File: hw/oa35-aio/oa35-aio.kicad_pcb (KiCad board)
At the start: 6 copper layers, 36 x 36 mm, 283 parts, among them J1 TYPE-C-31-M-12, J10 M1A, J11 M1B, J12 M1C, J13 M2A, J14 M2B, J15 M2C, J16 M3A, J17 M3B, J18 M3C, J19 M4A, J2 SM06B-SRSS-TB, J20 M4B, J21 M4C, J3 BAT+, J4 BAT-, P1 +5V, P10 TX6, P11 RX1, P12 TX1, P13 LED, P14 BZ-, P15 BZ+, P16 RSSI, P17 SCL, P18 SDA, P19 +3V3, P2 GND, P20 GND, P21 VBAT, P22 GND, P3 RX2, P4 TX2, P5 +5V, P6 GND, P7 RX4, P8 TX4, P9 RX6, Q1 2N7002, U1 INA186A3IDCKR, U10 USBLC6-2SC6, U2 LMR51430YFDDCR, U20 AT32F421G8U7, U21 NSG2065Q, U3 LMR51430YFDDCR, U30 AT32F421G8U7, U31 NSG2065Q, U4 LP5912-3.3DRVR, U40 AT32F421G8U7, U41 NSG2065Q, U5 TLV76733DRVR, U50 AT32F421G8U7, U51 NSG2065Q, U6 STM32F722RET6, U7 ICM-42688-P, U8 BMP280, U9 W25Q128JVSIQ, Y1 8MHz

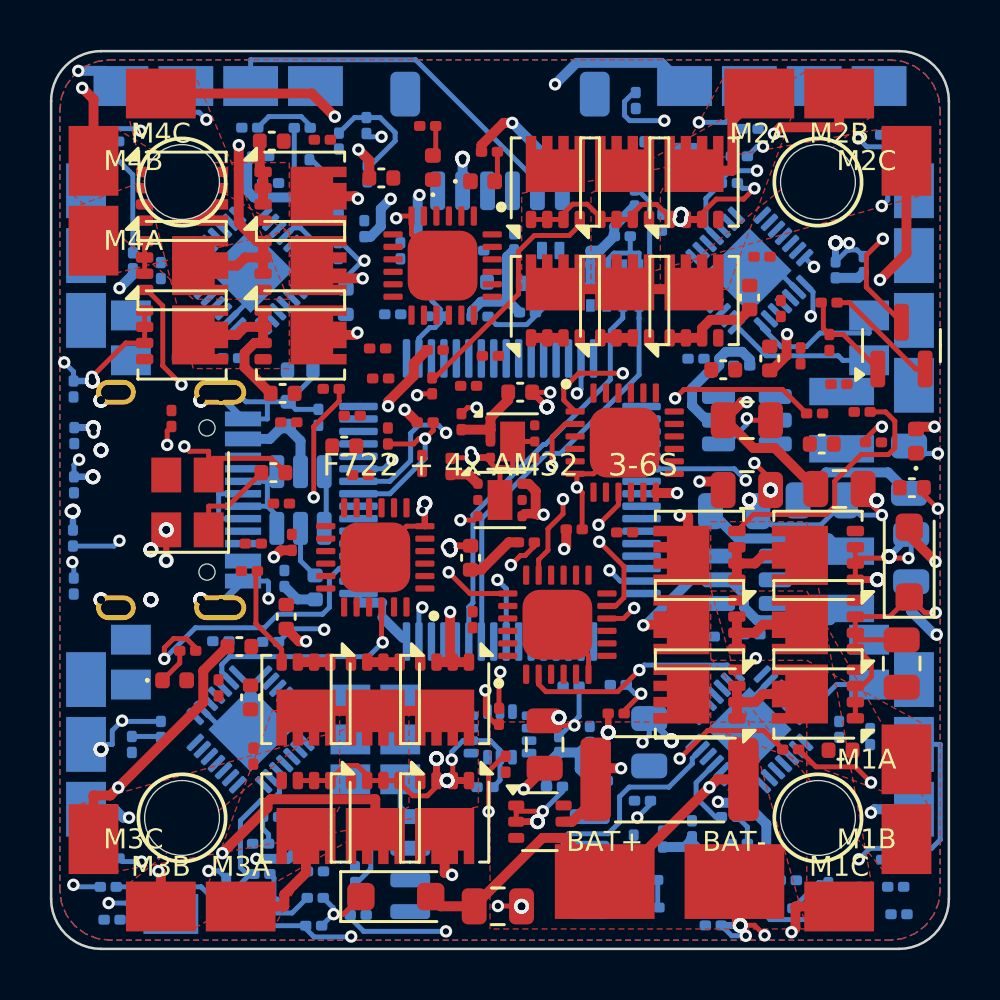
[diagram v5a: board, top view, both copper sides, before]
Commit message: OA35-AIO: leave the router's net classes alone, widen the power nets after
Rewriting the DSN class block to ask for wider phase and supply traces was
what made freerouting give up: with the rewritten block it routed 85 nets out
of 279, with KiCad's own block it routes them all. The high-current nets get
their copper back afterwards instead -- stitch.widen() fattens each segment
to as much as 0.8 mm wherever the surrounding geometry allows, testing the
widened shape against every other net before committing.

Co-Authored-By: Claude Opus 5 <noreply@anthropic.com>
Claude-Session: https://claude.ai/code/session_013J1rgXZWykCJN7jVVS67P2
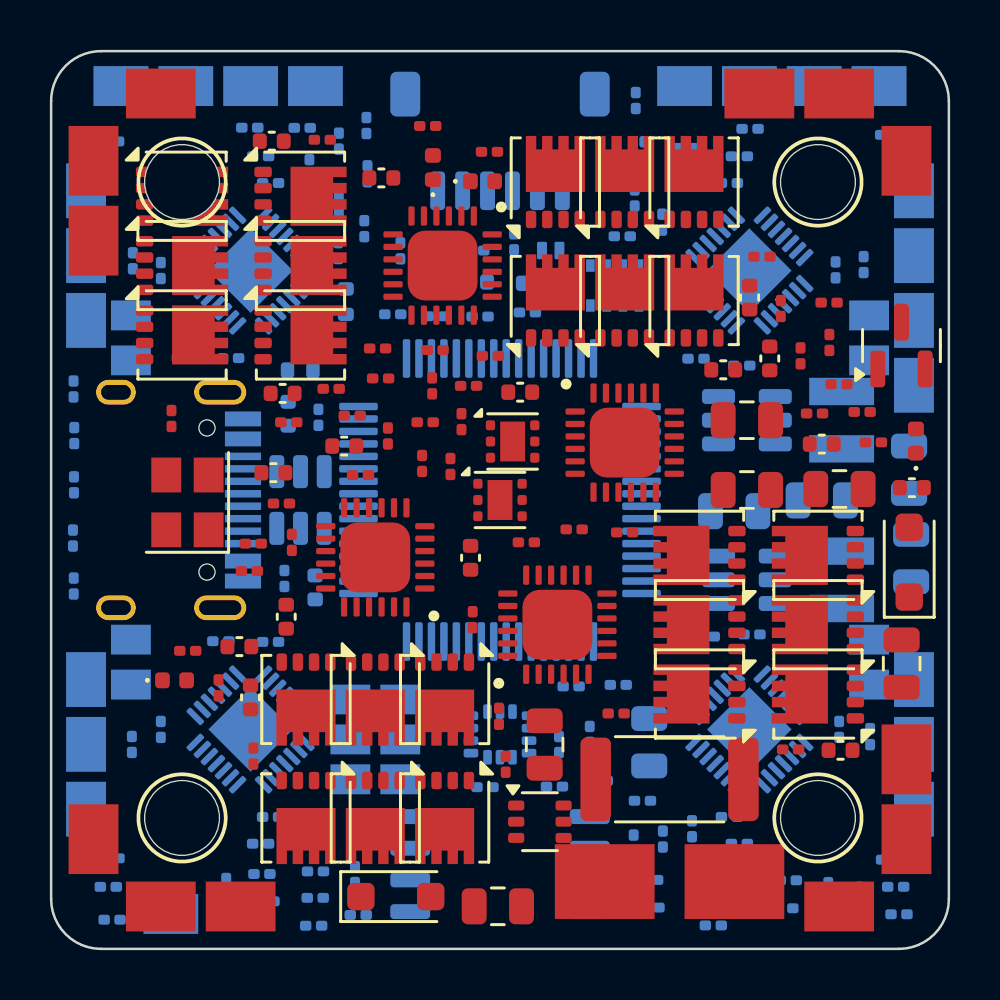
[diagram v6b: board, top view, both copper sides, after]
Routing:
- net GND: track 231.8 -> 0.00 mm, vias 129 -> 0
- net +5V: track 84.6 -> 0.00 mm, vias 6 -> 0
- net +3V3: track 46.5 -> 0.00 mm, vias 2 -> 0
- net PH_C_3: track 45.4 -> 0.00 mm, vias 4 -> 0
- net VBAT: track 45.0 -> 0.00 mm, vias 16 -> 0
- net PAD_BZ-: track 42.9 -> 0.00 mm, vias 2 -> 0
- net CURR: track 37.7 -> 0.00 mm, vias 3 -> 0
- net PAD_RSSI: track 37.3 -> 0.00 mm, vias 2 -> 0
- net ADC_RSSI: track 31.8 -> 0.00 mm, vias 2 -> 0
- net VBAT_IN: track 30.9 -> 0.00 mm, vias 2 -> 0
- net PH_B_4: track 30.1 -> 0.00 mm, vias 4 -> 0
- net PH_C_4: track 27.0 -> 0.00 mm, vias 2 -> 0
- net PH_B_3: track 26.1 -> 0.00 mm, vias 3 -> 0
- net PH_B_2: track 23.7 -> 0.00 mm, vias 2 -> 0
- net FBB_2: track 23.2 -> 0.00 mm, vias 2 -> 0
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- removed copper zone on B.Cu, net GND
- removed copper zone on F.Cu, net GND
- removed copper zone on In1.Cu, net GND
- removed copper zone on In3.Cu, net GND
- removed copper zone on In4.Cu, net GND
- removed copper zone on F.Cu, net PH_A_1
- removed copper zone on F.Cu, net PH_A_2
- removed copper zone on F.Cu, net PH_A_3
- removed copper zone on F.Cu, net PH_A_4
- removed copper zone on F.Cu, net PH_B_1
- removed copper zone on F.Cu, net PH_B_2
- removed copper zone on F.Cu, net PH_B_3
- removed copper zone on F.Cu, net PH_B_4
- removed copper zone on F.Cu, net PH_C_1
- removed copper zone on F.Cu, net PH_C_2
- removed copper zone on F.Cu, net PH_C_3
- removed copper zone on F.Cu, net PH_C_4
- removed copper zone on In2.Cu, net VBAT
- removed copper zone on F.Cu, net VBAT_IN
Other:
- board text removed: "+3V3"
- board text removed: "+5V"
- board text removed: "BAT+"
- board text removed: "BAT-"
- board text removed: "BOOT0"
- board text removed: "BZ+"
- board text removed: "BZ-"
- board text removed: "F722 + 4x AM32 3-6S"
- board text removed: "GND"
- board text removed: "LED"
- board text removed: "M1A"
- board text removed: "M1B"
- board text removed: "M1C"
- board text removed: "M2A"
- board text removed: "M2B"
- board text removed: "M2C"
- board text removed: "M3A"
- board text removed: "M3B"
- board text removed: "M3C"
- board text removed: "M4A"
- board text removed: "M4B"
- board text removed: "M4C"
- board text removed: "NRST"
- board text removed: "OA35-AIO rev A"
- board text removed: "RSSI"
- board text removed: "RX1"
- board text removed: "RX2"
- board text removed: "RX4"
- board text removed: "RX6"
- board text removed: "SCL"
- board text removed: "SDA"
- board text removed: "SWCLK"
- board text removed: "SWCLK1"
- board text removed: "SWCLK2"
- board text removed: "SWCLK3"
- board text removed: "SWCLK4"
- board text removed: "SWDIO"
- board text removed: "SWDIO1"
- board text removed: "SWDIO2"
- board text removed: "SWDIO3"
- board text removed: "SWDIO4"
- board text removed: "TX1"
- board text removed: "TX2"
- board text removed: "TX4"
- board text removed: "TX6"
- board text removed: "VBAT"

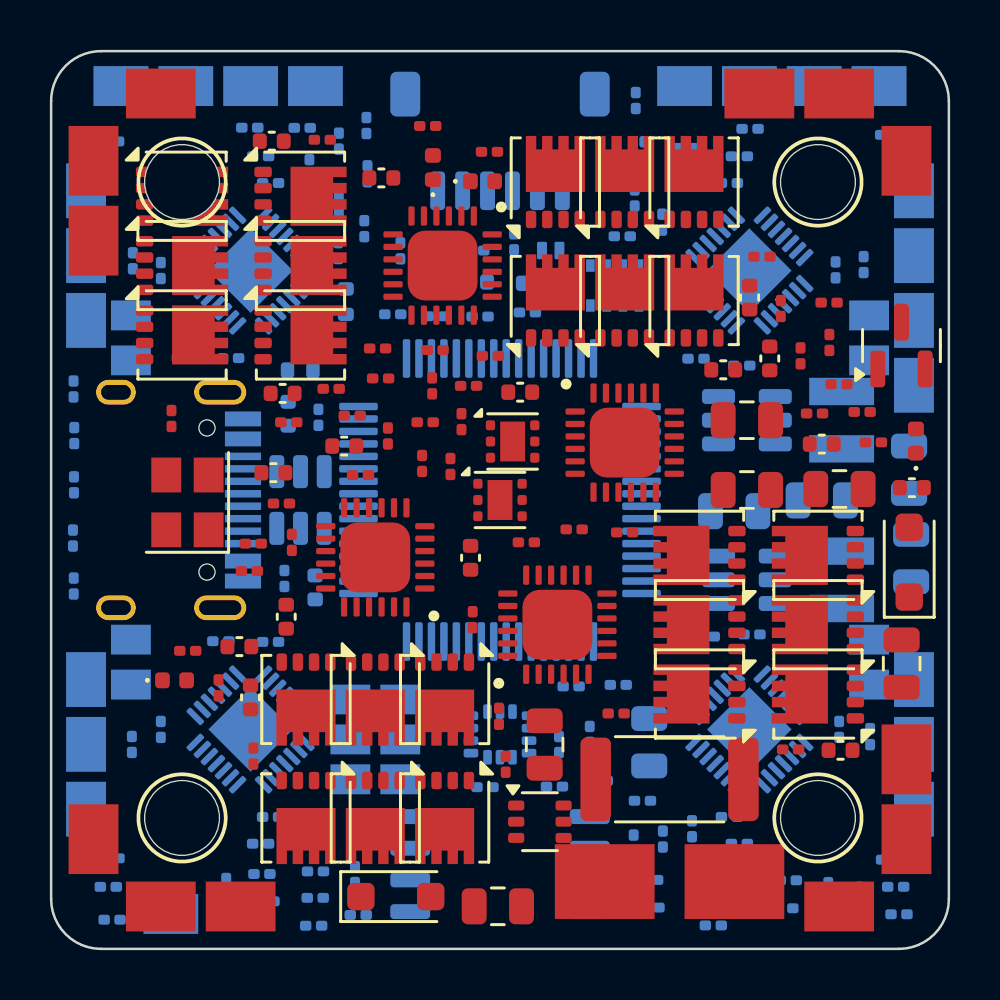
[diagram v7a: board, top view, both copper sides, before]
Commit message: OA35-AIO: route to JLCPCB's 5 mil rules instead of 0.2/0.15
At 0.2 mm track and 0.15 mm clearance there is no channel between the pins of
a 0.4 mm pitch QFN, which is why the autorouter kept leaving about a third of
the nets bare whatever else was changed. 0.13/0.13 is JLCPCB's standard
capability; the current-carrying nets are fattened again afterwards by
stitch.widen().

Co-Authored-By: Claude Opus 5 <noreply@anthropic.com>
Claude-Session: https://claude.ai/code/session_013J1rgXZWykCJN7jVVS67P2
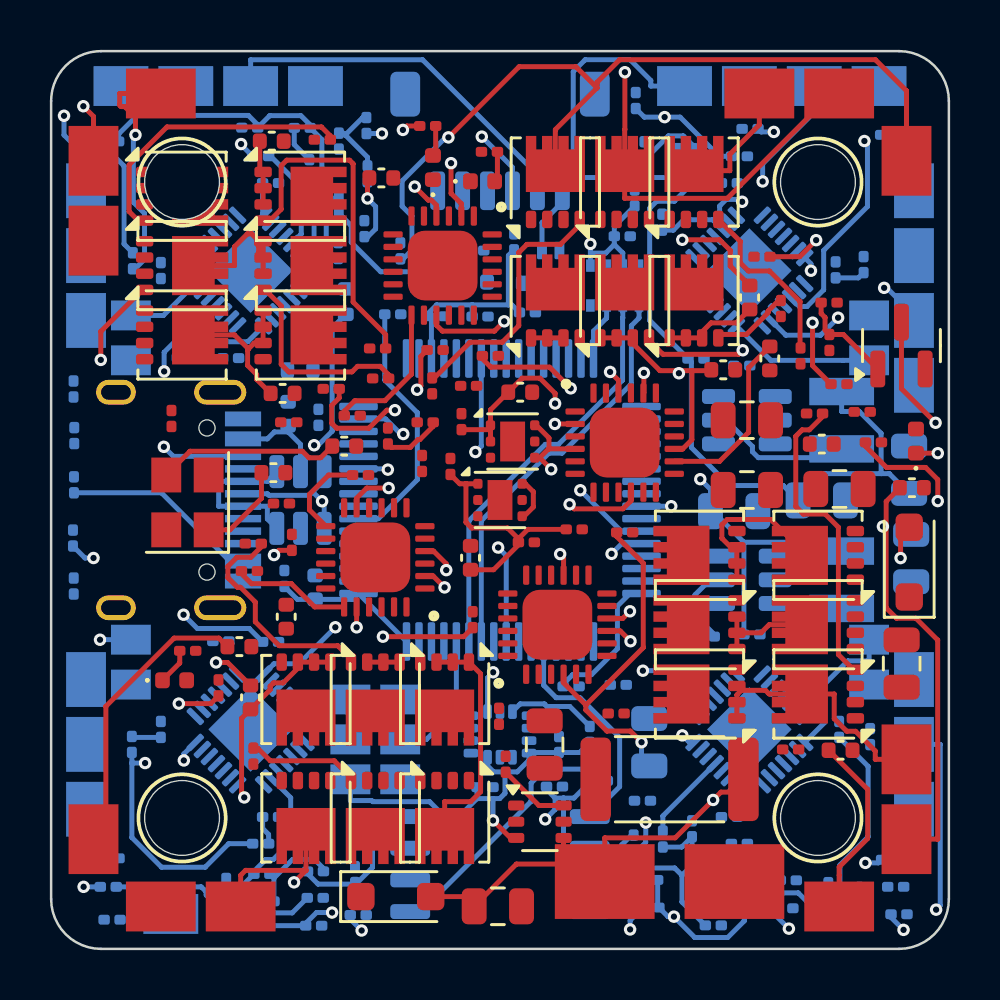
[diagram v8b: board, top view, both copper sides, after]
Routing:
- net +3V3E: track 0.00 -> 114.1 mm, vias 0 -> 6
- net +10V: track 0.00 -> 90.3 mm, vias 0 -> 8
- net +3V3: track 0.00 -> 78.3 mm, vias 0 -> 4
- net PH_B_1: track 0.00 -> 49.6 mm, vias 0 -> 3
- net PH_B_2: track 0.00 -> 38.1 mm, vias 0 -> 2
- net UART1_RX: track 0.00 -> 37.3 mm, vias 0 -> 3
- net PAD_RSSI: track 0.00 -> 35.3 mm, vias 0 -> 2
- net PH_C_2: track 0.00 -> 35.3 mm, vias 0 -> 1
- net PH_B_4: track 0.00 -> 34.9 mm, vias 0 -> 3
- net PAD_BZ-: track 0.00 -> 32.3 mm, vias 0 -> 2
- net VBAT_IN: track 0.00 -> 31.7 mm, vias 0 -> 2
- net ADC_RSSI: track 0.00 -> 29.8 mm, vias 0 -> 2
- net +5V_BUCK: track 0.00 -> 28.7 mm
- net UART4_RX: track 0.00 -> 25.9 mm, vias 0 -> 2
- net FBB_1: track 0.00 -> 25.8 mm, vias 0 -> 3
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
